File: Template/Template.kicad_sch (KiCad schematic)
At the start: 19 parts

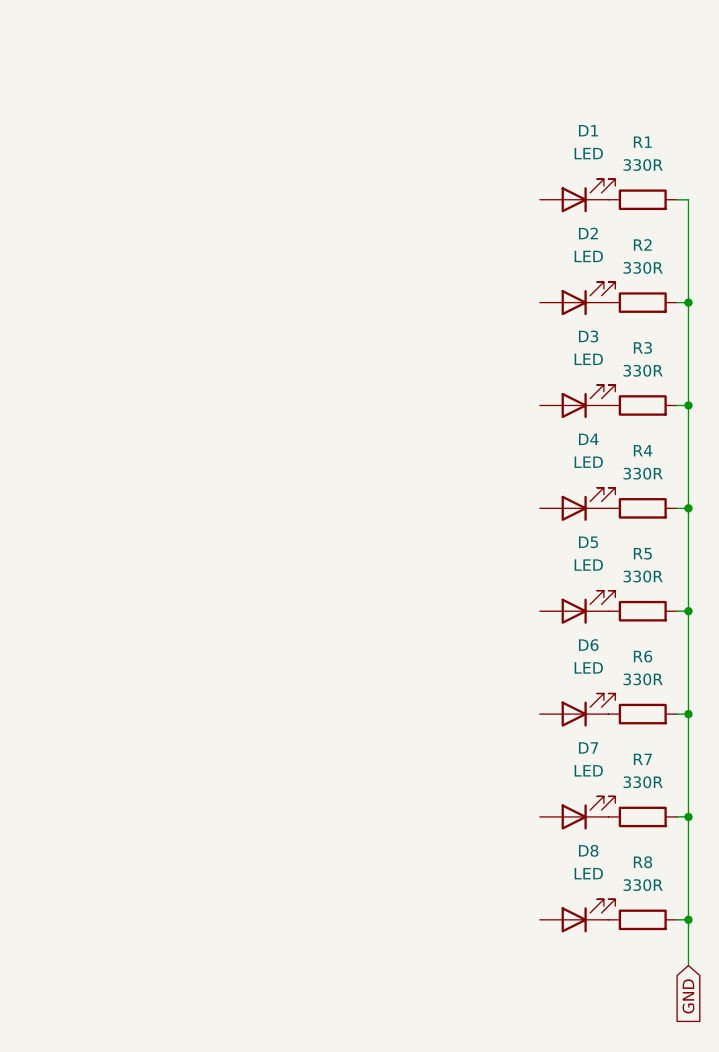
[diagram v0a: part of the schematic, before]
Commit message: [Template] - clarified the MSB/LSB order for the indicator LEDs.
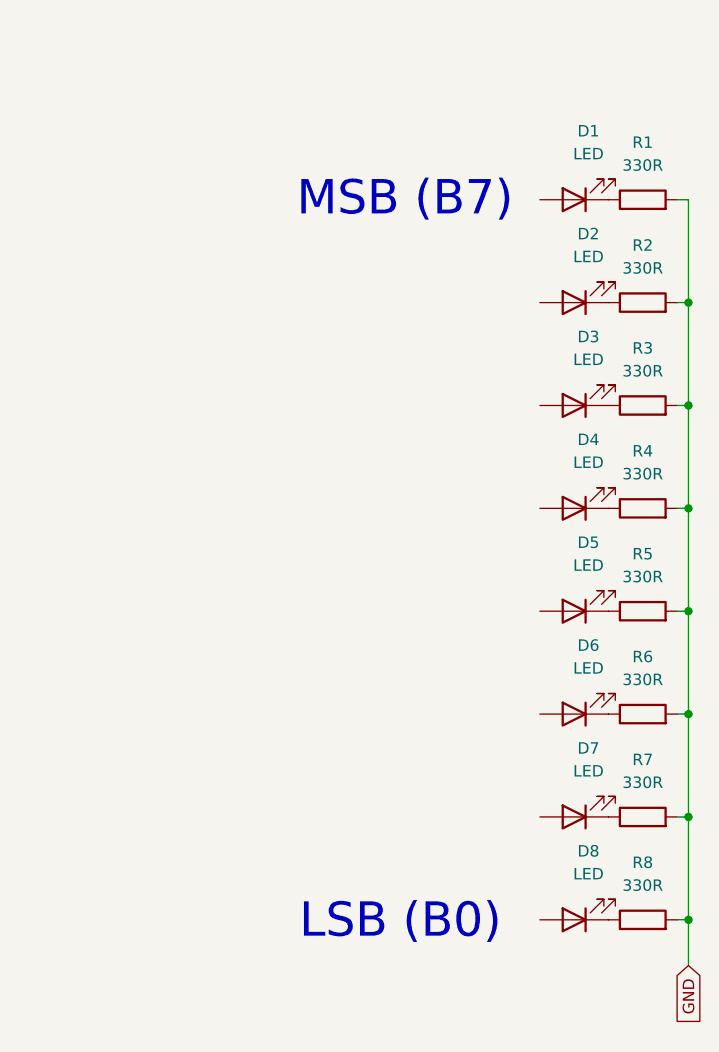
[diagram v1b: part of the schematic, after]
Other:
- note added: "LSB (B0)"
- note added: "MSB (B7)"
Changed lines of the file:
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@@
 		(company "D. Q. McDonald")
+	)
+	(text "LSB (B0)"
+		(exclude_from_sim no)
+		(at 248.666 152.654 0)
+		(effects
+			(font
+				(size 3.81 3.81)
+			)
+		)
+	)
+	(text "MSB (B7)"
+		(exclude_from_sim no)
+		(at 249.174 72.39 0)
+		(effects
+			(font
+				(size 3.81 3.81)
+			)
+		)
 	)
 	(junction

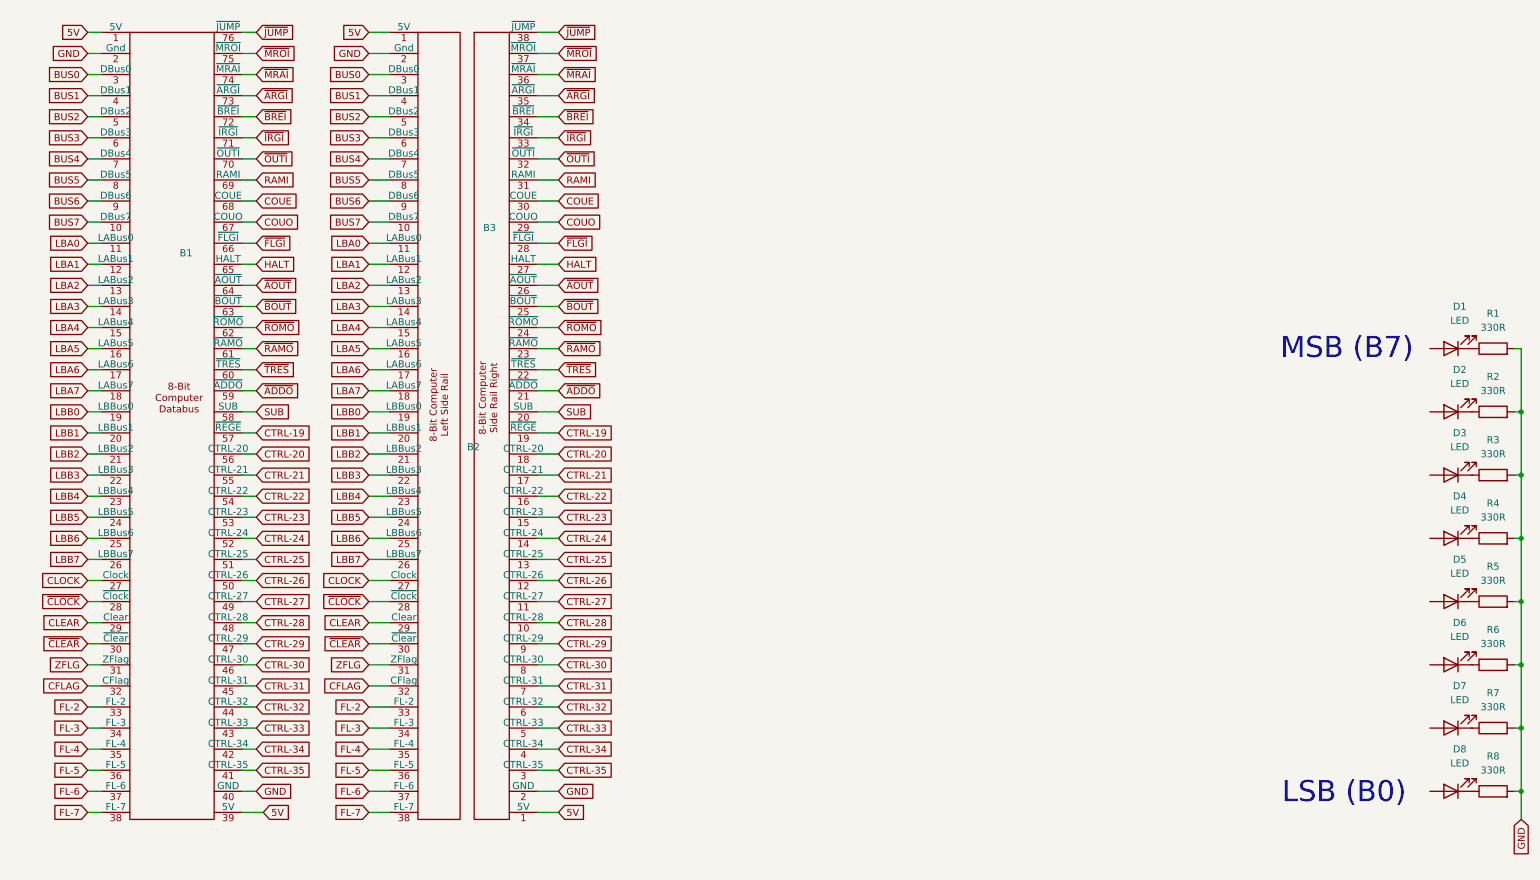
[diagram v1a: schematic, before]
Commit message: [Template] - added PWR_FLAGS to 5V and GND pins on backplane.
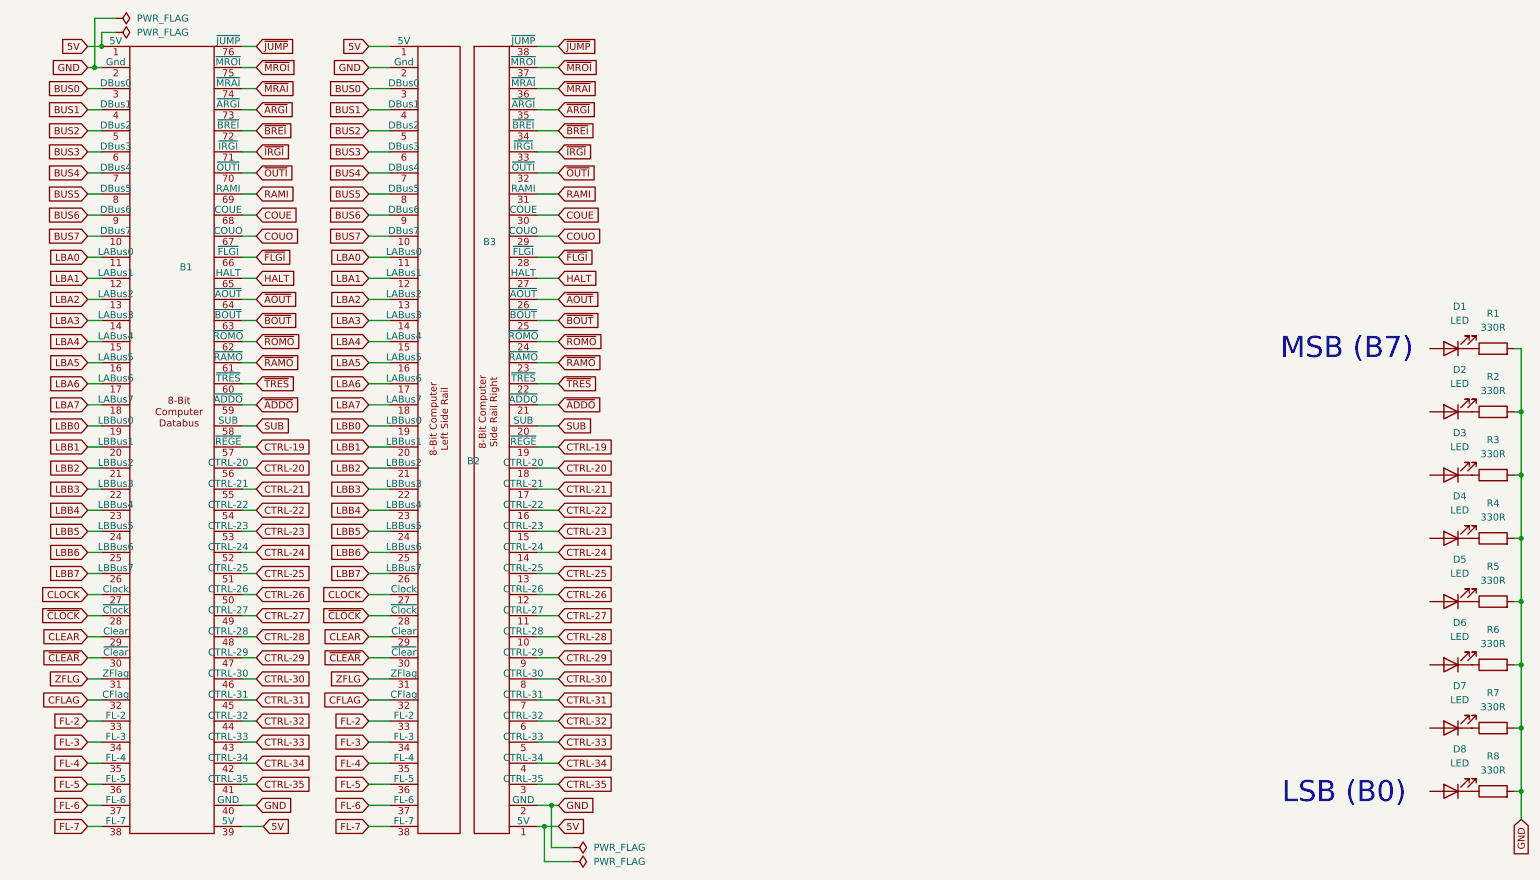
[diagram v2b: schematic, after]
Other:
- moved on the sheet: B1, B2, B3

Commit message: [Template] - fixed annoying DRC errors with silkscreen. Added second set of carry and zero flags.
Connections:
- net FL-2 renamed ZFLAG2
- net FL-3 renamed CFLAG2
- net ZFLG renamed ZFLAG
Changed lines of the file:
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@@
 		)
 	)
-	(global_label "FL-3"
+	(global_label "CFLAG2"
 		(shape input)
 		(at 72.39 143.51 180)
@@
 		)
 		(property "Intersheetrefs" "${INTERSHEET_REFS}"
-			(at 64.5062 143.51 0)
+			(at 62.45 143.51 0)
 			(hide yes)
 			(show_name no)
@@
 		)
 	)
-	(global_label "FL-2"
+	(global_label "ZFLAG2"
 		(shape input)
 		(at 72.39 139.7 180)
@@
 		)
 		(property "Intersheetrefs" "${INTERSHEET_REFS}"
-			(at 64.5062 139.7 0)
+			(at 62.5105 139.7 0)
 			(hide yes)
 			(show_name no)
@@
 		)
 	)
-	(global_label "ZFLG"
+	(global_label "ZFLAG"
 		(shape input)
 		(at 21.59 132.08 180)
@@
 		)
 		(property "Intersheetrefs" "${INTERSHEET_REFS}"
-			(at 14.0086 132.08 0)
+			(at 12.92 132.08 0)
 			(hide yes)
 			(show_name no)
@@
 		)
 	)
-	(global_label "FL-2"
+	(global_label "ZFLAG2"
 		(shape input)
 		(at 21.59 139.7 180)
@@
 		)
 		(property "Intersheetrefs" "${INTERSHEET_REFS}"
-			(at 13.7062 139.7 0)
+			(at 11.7105 139.7 0)
 			(hide yes)
 			(show_name no)
@@
 		)
 	)
-	(global_label "FL-3"
+	(global_label "CFLAG2"
 		(shape input)
 		(at 21.59 143.51 180)
@@
 		)
 		(property "Intersheetrefs" "${INTERSHEET_REFS}"
-			(at 13.7062 143.51 0)
+			(at 11.65 143.51 0)
 			(hide yes)
 			(show_name no)
@@
 		)
 	)
-	(global_label "ZFLG"
+	(global_label "ZFLAG"
 		(shape input)
 		(at 72.39 132.08 180)
@@
 		)
 		(property "Intersheetrefs" "${INTERSHEET_REFS}"
-			(at 64.8086 132.08 0)
-			(hide yes)
-			(show_name no)
+			(at 63.72 132.08 0)
+			(hide yes)
+			(show_name no)

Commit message: [Template] - updated for COUO being inverted signal  Please enter the commit message for your changes. Lines starting
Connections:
- net COUO renamed ~{COUO}
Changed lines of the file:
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@@
 		)
 	)
-	(global_label "COUO"
+	(global_label "~{COUO}"
 		(shape input)
 		(at 106.68 52.07 0)
@@
 		)
 	)
-	(global_label "COUO"
+	(global_label "~{COUO}"
 		(shape input)
 		(at 52.07 52.07 0)
